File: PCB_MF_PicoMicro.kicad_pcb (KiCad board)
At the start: 2 copper layers, 36.5 x 18.5 mm, 39 parts, among them J3 USB_C_Receptacle_USB2.0_16P, J7 Conn_01x02_Pin, J8 Conn_01x02_Pin, SW1 SW_Push, U1 RP2040, U2 AMS1117-3.3, U4 W25Q16JVSS, U5 ProMicro, Y1 X322512MSB4SI

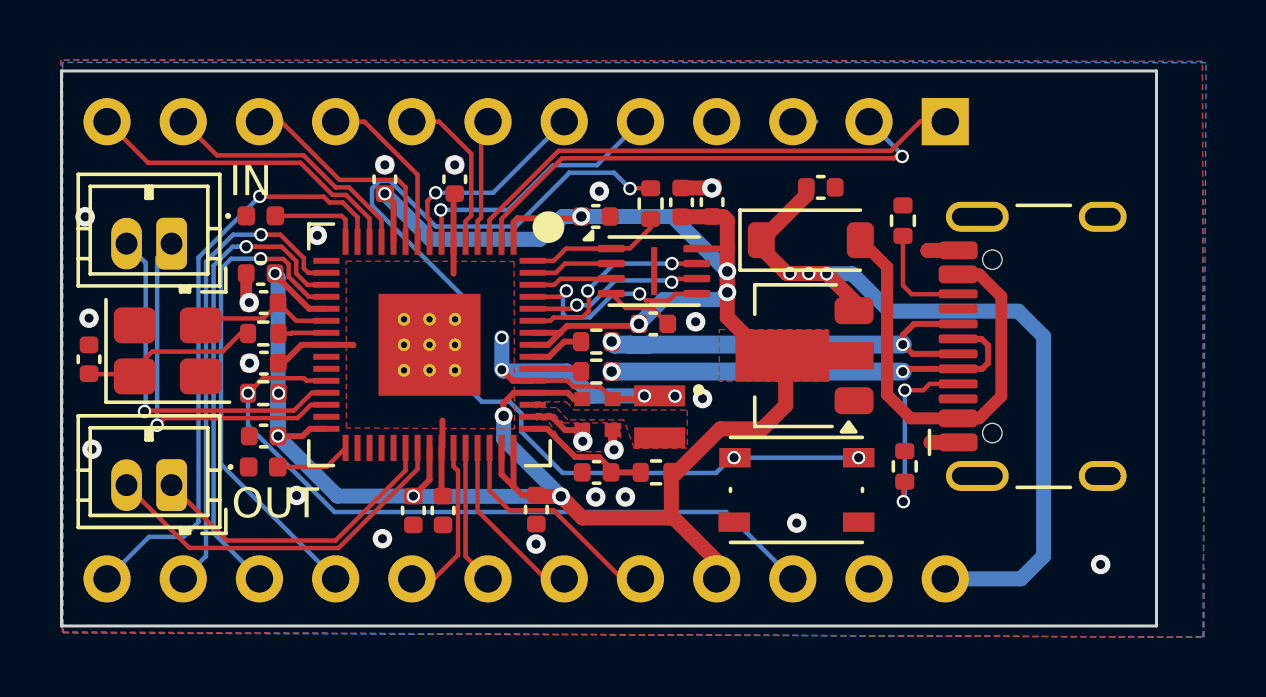
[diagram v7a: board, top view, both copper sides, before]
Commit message: add missing R for LEDs, add production files for JLCPCB
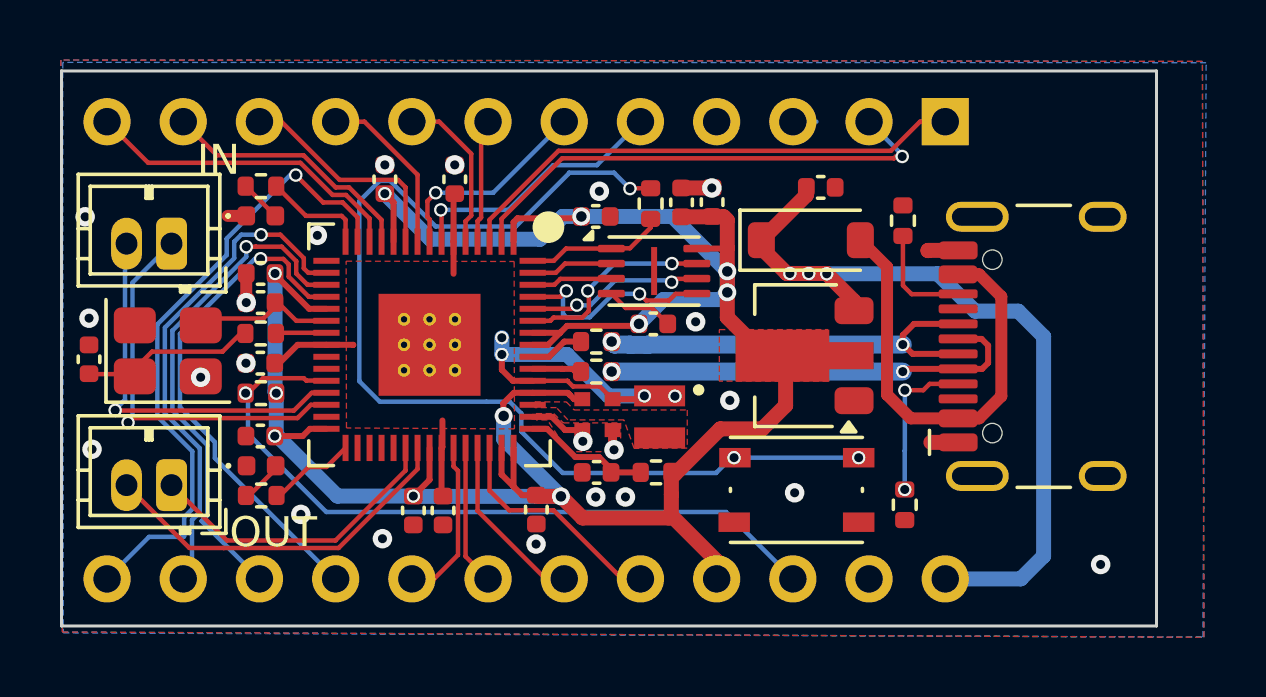
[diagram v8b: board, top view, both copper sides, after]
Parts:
- added R10: 150, Resistor_SMD:R_0402_1005Metric, F.Cu at (111.9, 95.6)
- added R9: 150, Resistor_SMD:R_0402_1005Metric, F.Cu at (111.9, 85.3)
- moved R7 1.28 mm to (133.3, 95.9), turned to 90 degrees
- moved C7 0.12 mm to (111.9, 91.2)
- moved C12 0.11 mm to (111.9, 93.6)
- moved C4 0.10 mm to (111.9, 89.1)
- moved R2 0.09 mm to (111.9, 90.2)
- moved D2 0.08 mm to (111.9, 94.6)
- moved R6 0.08 mm to (111.9, 92.2)
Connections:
- D2 pad 2: /RP2350A/GPIO19 -> Net-(D2-A)
- D3 pad 2: /RP2350A/GPIO11 -> Net-(D3-A)
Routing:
- net /RP2350A/~{USB_BOOT}: track 33.8 -> 36.1 mm
- net Net-(D2-A): track 0.00 -> 1.56 mm
- net Net-(D3-A): track 0.00 -> 1.40 mm
- net D10: track 19.9 -> 21.3 mm
- net RX1: track 12.2 -> 13.4 mm
- net Net-(J3-CC1): track 6.28 -> 5.17 mm
- net D14: track 16.3 -> 17.3 mm
- net 3.3V: track 84.8 -> 83.9 mm
- net D13: track 16.0 -> 16.8 mm
- net TX1: track 12.2 -> 13.0 mm
- net D15: track 16.4 -> 17.1 mm
- net GND: track 10.3 -> 10.9 mm, vias 21 -> 22
